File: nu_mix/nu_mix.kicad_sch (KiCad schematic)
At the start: 63 parts, among them J1 2X5, J2 I/O connector, J3 I/O connector, Q1 LBSS84LT1G, SW1 SW_DP3T, SW2 SW_DP3T, SW3 SW_DP3T, SW4 SW_DP3T, SW5 SW_DP3T, SW6 SW_DP3T, SW7 SW_DP3T, SW8 SW_DP3T, U1 OPA202IDBVR, U2 OPA2202IDGKR

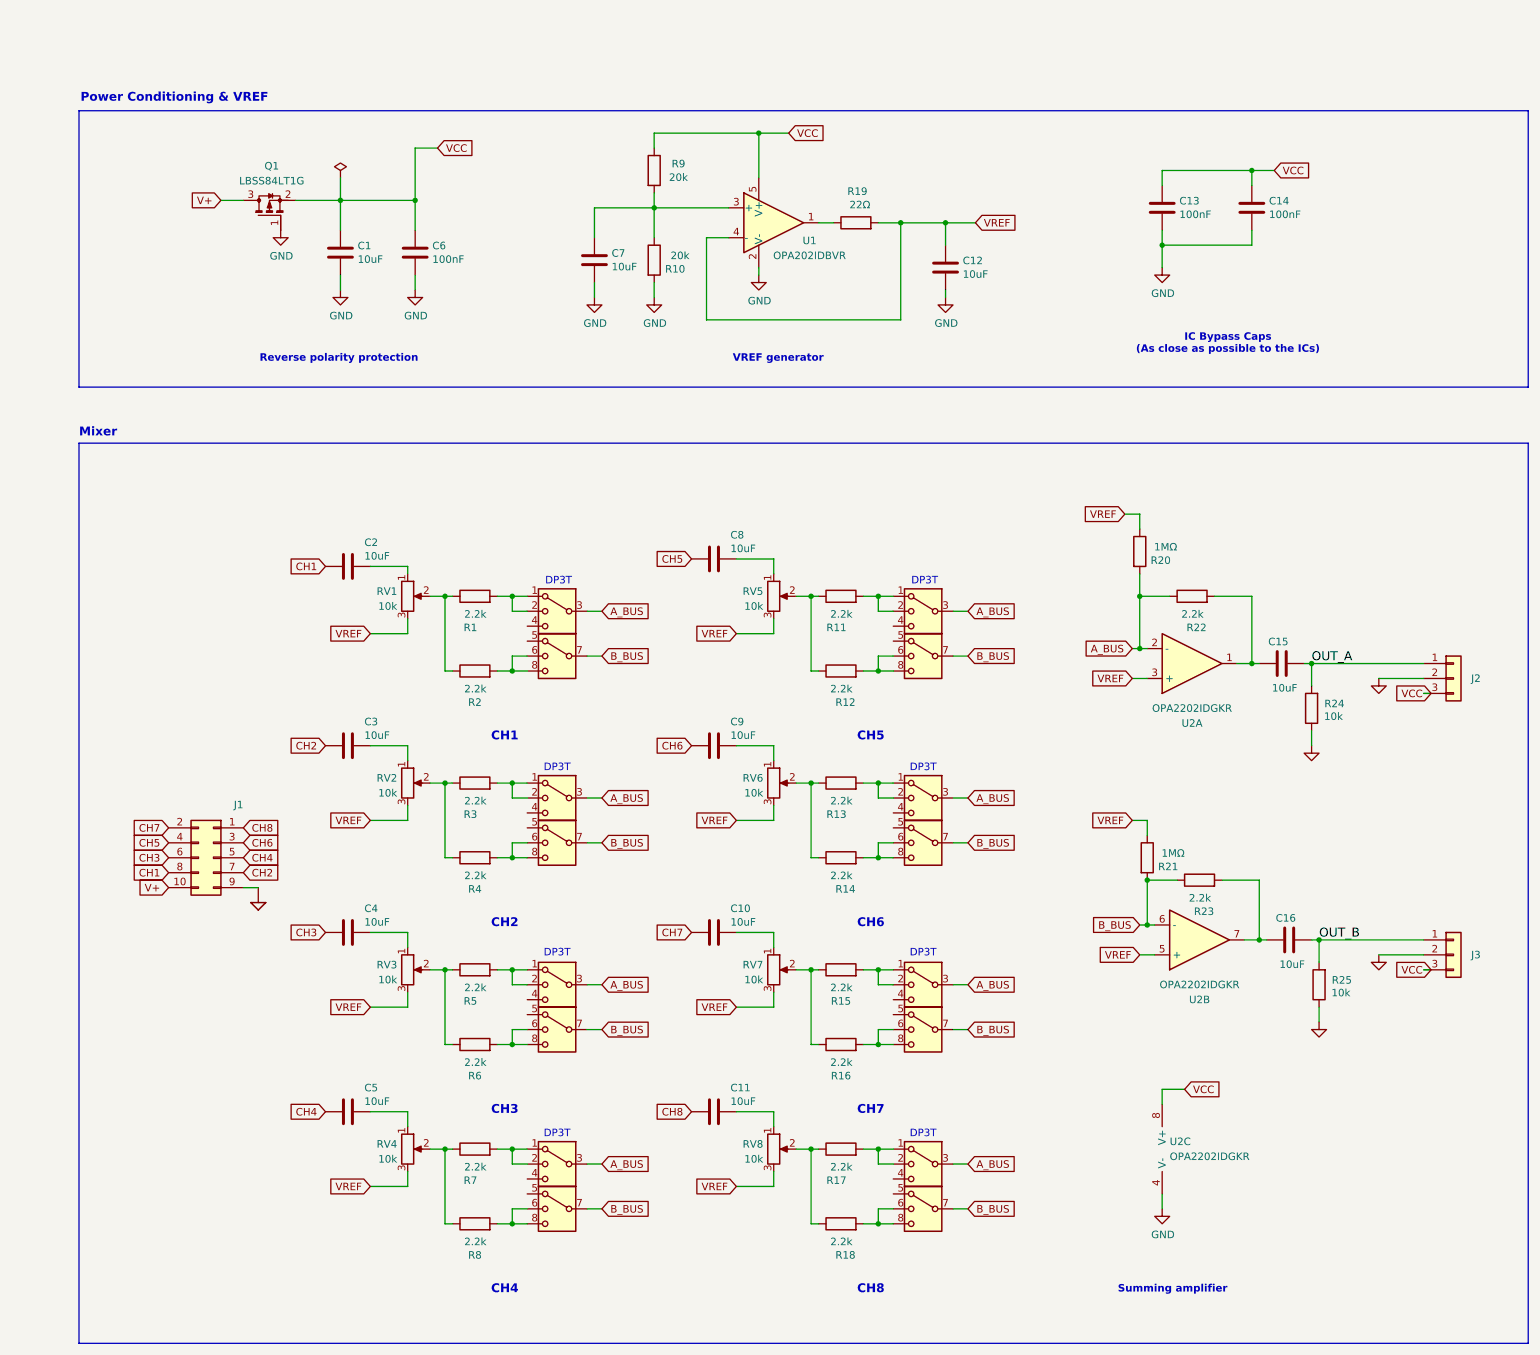
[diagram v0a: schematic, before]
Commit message: - Complete schematics - Start PCB layout - Switch to shorter 20mm sliders
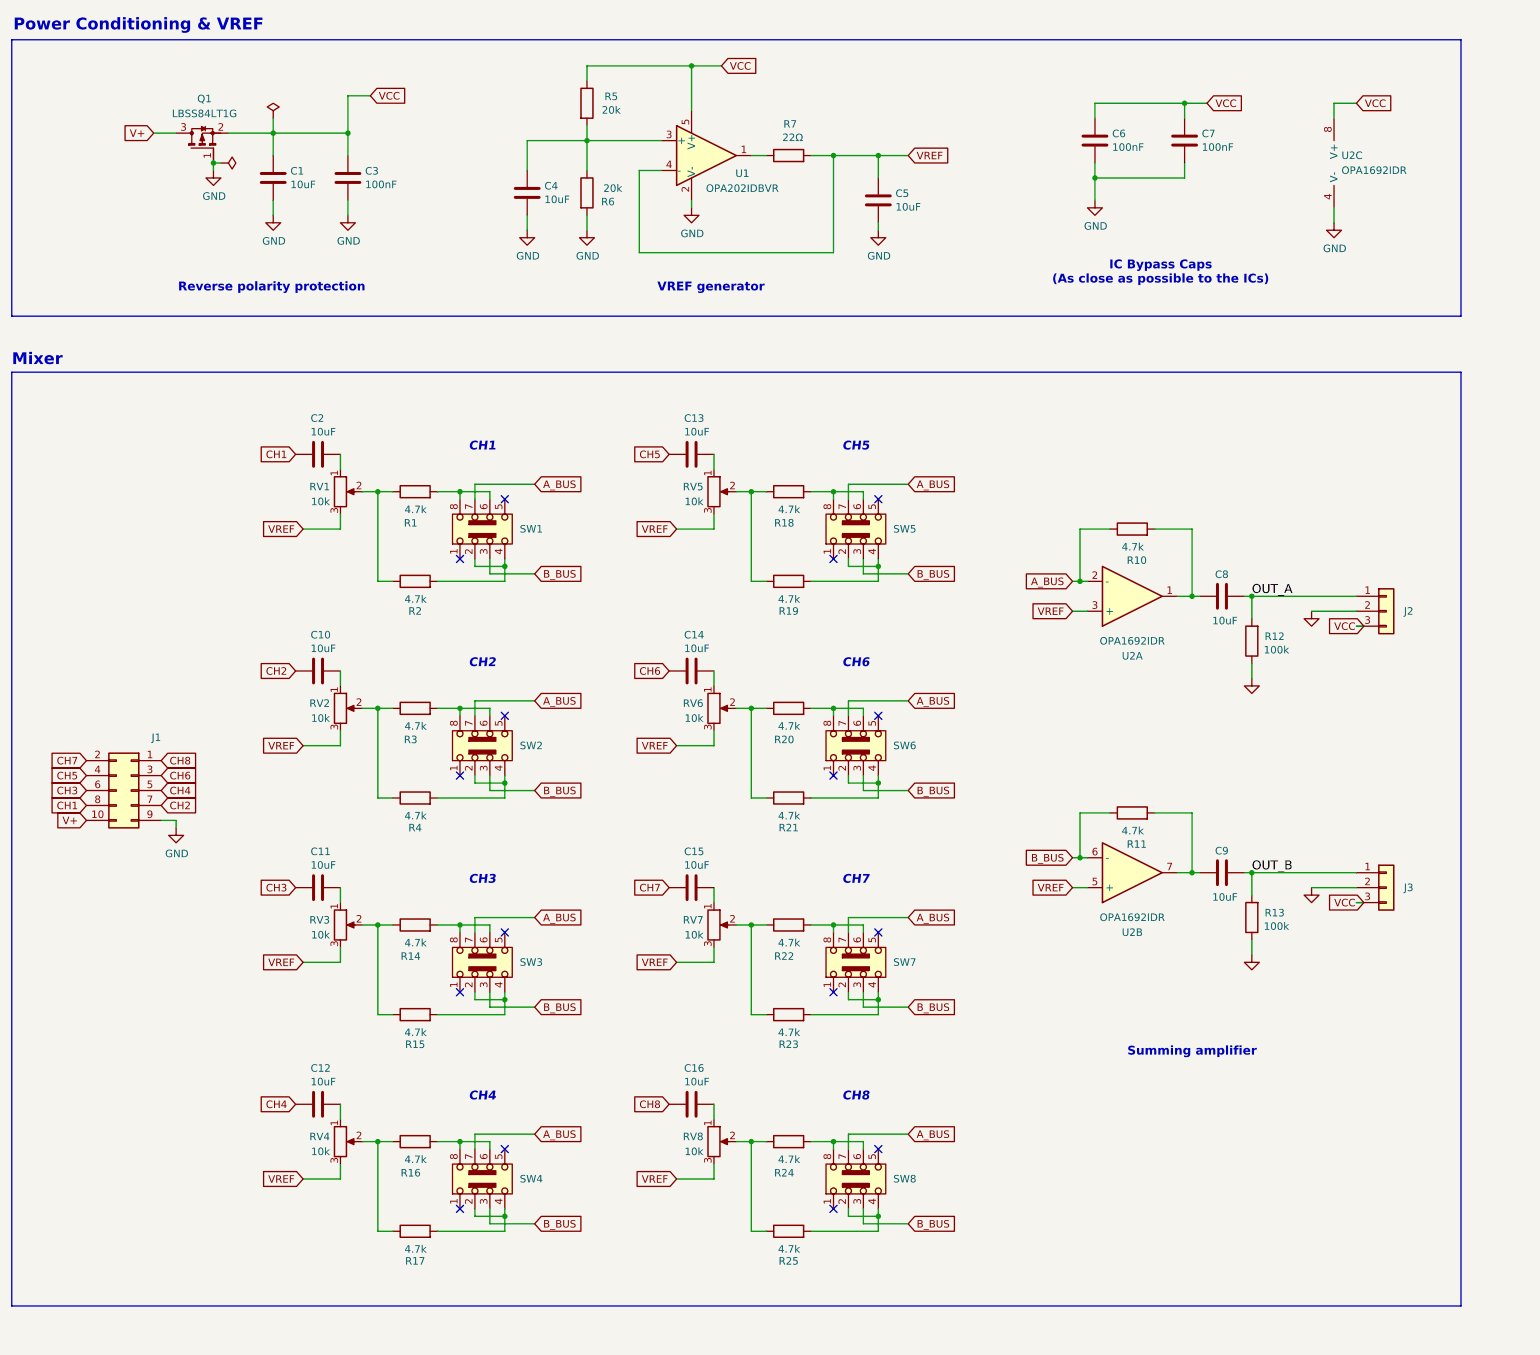
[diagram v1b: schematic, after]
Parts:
- removed C2, C3, C4, C5, C9: 10uF, Capacitor_SMD:C_0603_1608Metric, symbol Device:C
- removed R1, R13, R2, R5, R6, R7, R8: 2.2k, Resistor_SMD:R_0402_1005Metric, symbol Device:R
- removed RV1: 10k, cycfi_library:Alps_RS301111A01G, symbol Device:R_Potentiometer
- removed SW1, SW2, SW3, SW4, SW5, SW6, SW7, SW8: SW_DP3T, symbol Switch:SW_DP3T
- added C12, C13, C14, C15, C16: 10uF, Capacitor_SMD:C_0603_1608Metric, symbol Device:C
- added R19, R22, R23, R24, R25: 4.7k, Resistor_SMD:R_0402_1005Metric, symbol Device:R
- added RV5: 10k, cycfi_library:Alps_RS201111J011, symbol Device:R_Potentiometer
- added SW1, SW2, SW3, SW4, SW5, SW6, SW7, SW8: SW_Slide_DP3T, cycfi_library:K3-1400S-D1, symbol cycfi_library:SW_Slide_DP3T
- R1: renamed from R11; value 2.2k -> 4.7k; LCSC C25879 -> C25900
- R10: renamed from R22; value 2.2k -> 4.7k; LCSC C25879 -> C25900
- R11: renamed from R23; value 2.2k -> 4.7k; LCSC C25879 -> C25900
- R12: renamed from R24; value 10k -> 100k; LCSC C25744 -> C25741
- R13: renamed from R25; value 10k -> 100k; LCSC C25744 -> C25741
- R14, R15, R16, R17, R18, R3, R4: value 2.2k -> 4.7k; LCSC C25879 -> C25900
- R2: renamed from R12; value 2.2k -> 4.7k; LCSC C25879 -> C25900
- R20, R21: value 1MΩ -> 4.7k; LCSC C26083 -> C25900
- RV1: renamed from RV5; footprint cycfi_library:Alps_RS301111A01G -> cycfi_library:Alps_RS201111J011; LCSC (none) -> C255504
- RV2, RV3, RV4, RV6, RV7, RV8: footprint cycfi_library:Alps_RS301111A01G -> cycfi_library:Alps_RS201111J011; LCSC (none) -> C255504
- U1: LCSC (none) -> C1850244
- U2: value OPA2202IDGKR -> OPA1692IDR; footprint (none) -> Package_SO:SOIC-8_3.9x4.9mm_P1.27mm; LCSC (none) -> C2060550
- renumbered C8 to C2, C6 to C3, C7 to C4, C12 to C5, C13 to C6, C14 to C7, C15 to C8, C16 to C9, R9 to R5, R10 to R6, R19 to R7
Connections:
- net A_BUS: now also SW1.7 (C2), SW2.7 (C2), SW3.7 (C2), SW4.7 (C2), SW5.7 (C2), SW6.7 (C2), SW7.7 (C2), SW8.7 (C2); no longer R20.2
- net B_BUS: now also SW1.3 (C1`), SW2.3 (C1`), SW3.3 (C1`), SW4.3 (C1`), SW5.3 (C1`), SW6.3 (C1`), SW7.3 (C1`), SW8.3 (C1`); no longer R21.2
- net CH1: now also C2.1
- net CH2: now also C10.1
- net CH3: now also C11.1
- net CH4: now also C12.1
- net CH5: now also C13.1; no longer C2.1
- net CH6: now also C14.1
- net CH7: now also C15.1; no longer C10.1
- net CH8: now also C16.1; no longer C11.1
- net VREF: now also RV5.3; no longer R20.1, R21.1
- net at R3.2: now also SW2.6 (C2`), SW2.8 (A2)
- net at R16.2: now also SW4.6 (C2`), SW4.8 (A2)
- net at R4.2: now also SW2.2 (C1), SW2.4 (B1)
- net at RV4.2: now also R16.1, R17.1
- net at RV4.1: now also C12.2
- net at R17.2: now also SW4.2 (C1), SW4.4 (B1)
- net at R14.2: now also SW3.6 (C2`), SW3.8 (A2)
- net at R1.2: now also SW1.6 (C2`), SW1.8 (A2)
- net at C10.2: now also RV2.1; no longer RV7.1
- net at RV6.1: now also C14.2
- net at RV6.2: now also R20.1, R21.1; no longer R14.1
- net at RV8.1: now also C16.2; no longer C11.2
- net at R15.2: now also SW3.2 (C1), SW3.4 (B1)
- net at RV3.1: now also C11.2
- net at R18.2: now also SW5.6 (C2`), SW5.8 (A2)
- net at R2.2: now also SW1.2 (C1), SW1.4 (B1)
- net at RV3.2: now also R14.1, R15.1
- new net: R20.2, SW6.6 (C2`), SW6.8 (A2)
- new net: R23.2, SW7.2 (C1), SW7.4 (B1)
- new net: R22.2, SW7.6 (C2`), SW7.8 (A2)
- new net: R21.2, SW6.2 (C1), SW6.4 (B1)
- new net: R22.1, R23.1, RV7.2
- new net: C15.2, RV7.1
- new net: R18.1, R19.1, RV5.2
- new net: R19.2, SW5.2 (C1), SW5.4 (B1)
- new net: C13.2, RV5.1
- new net: R24.1, R25.1, RV8.2
- new net: R24.2, SW8.6 (C2`), SW8.8 (A2)
- new net: R25.2, SW8.2 (C1), SW8.4 (B1)
- no-connect marks 0 -> 16
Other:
- note removed: "DP3T"
- moved on the sheet: C1, C2, C3, C4, C5, C6, C7, C8, C9, J1, J2, J3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

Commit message: Full layout
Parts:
- J1: footprint Connector_PinHeader_2.00mm:PinHeader_2x05_P2.00mm_Vertical -> cycfi_library:pin_header_2x5p_2.54mm_smd_horizontal
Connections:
- net A_BUS: now also SW1.3 (C1`), SW2.3 (C1`), SW3.3 (C1`), SW4.3 (C1`), SW5.3 (C1`), SW6.3 (C1`), SW7.3 (C1`), SW8.3 (C1`); no longer SW1.7 (C2), SW2.7 (C2), SW3.7 (C2), SW4.7 (C2), SW5.7 (C2), SW6.7 (C2), SW7.7 (C2), SW8.7 (C2)
- net B_BUS: now also SW1.7 (C2), SW2.7 (C2), SW3.7 (C2), SW4.7 (C2), SW5.7 (C2), SW6.7 (C2), SW7.7 (C2), SW8.7 (C2); no longer SW1.3 (C1`), SW2.3 (C1`), SW3.3 (C1`), SW4.3 (C1`), SW5.3 (C1`), SW6.3 (C1`), SW7.3 (C1`), SW8.3 (C1`)
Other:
- moved on the sheet: R1, R14, R15, R16, R17, R18, R19, R2, R20, R21, R22, R23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

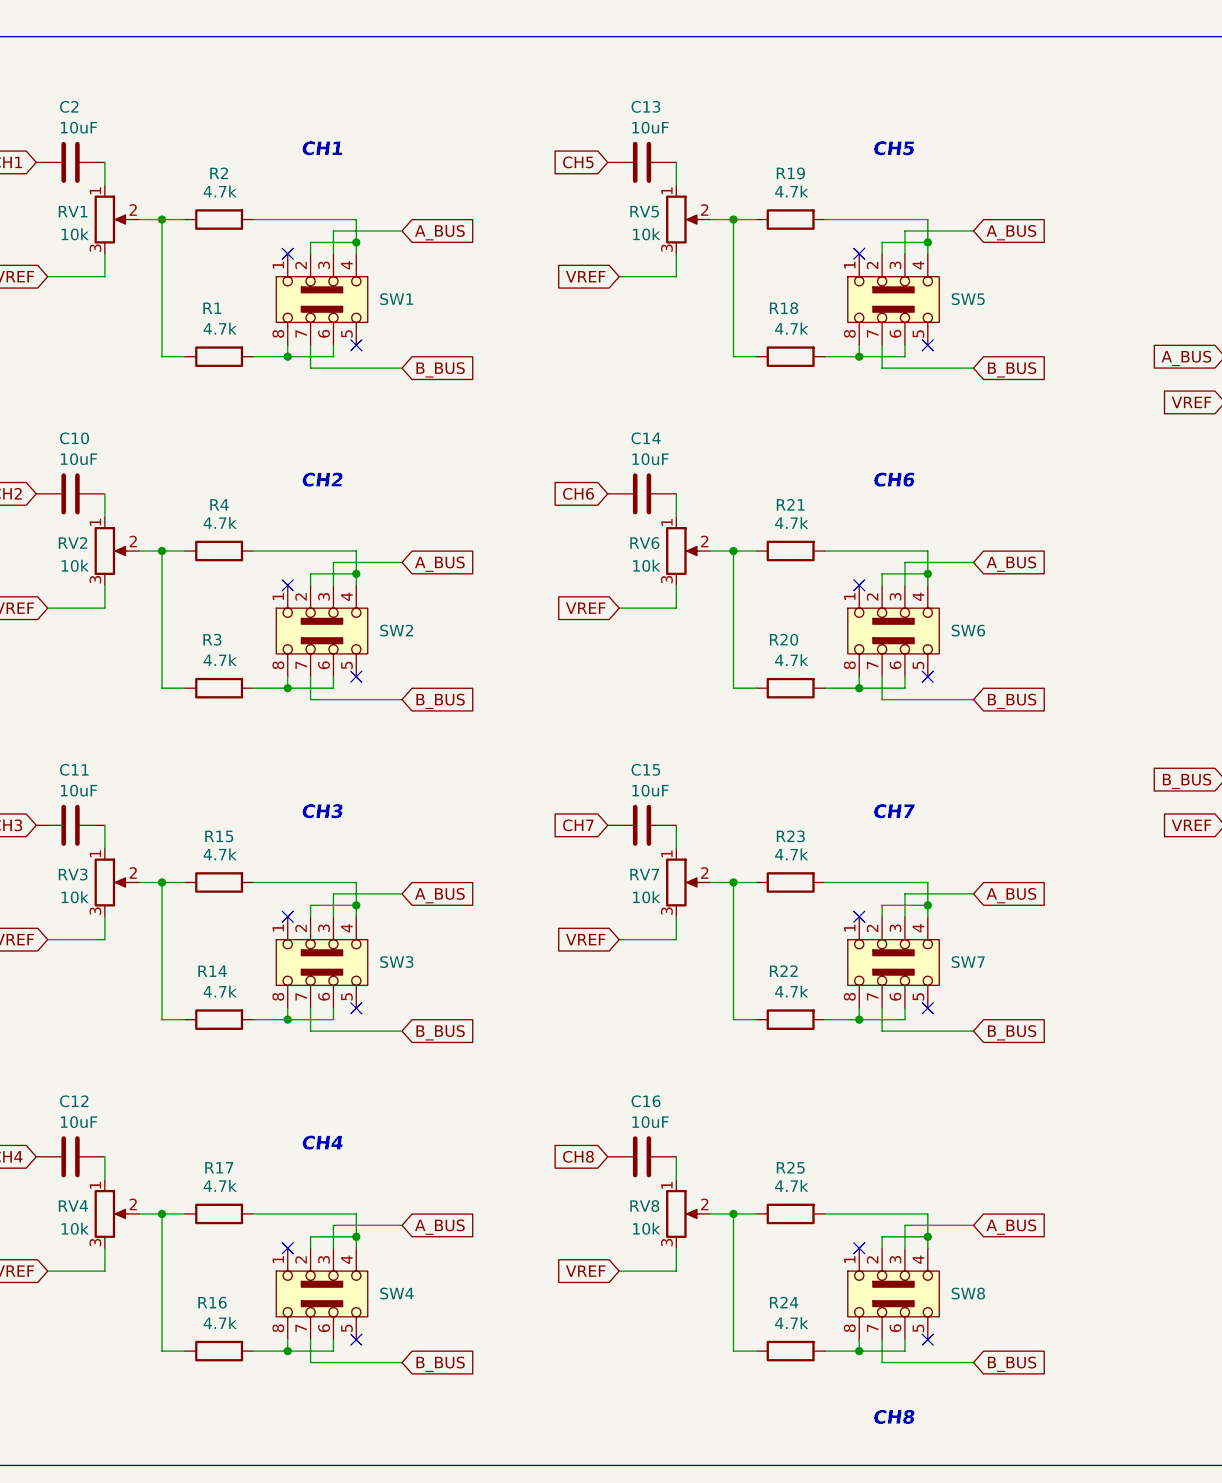
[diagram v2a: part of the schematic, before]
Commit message: Fix orientation of the slide switches so A is at the left and B is at the right in both the schematic diagram and the PCB
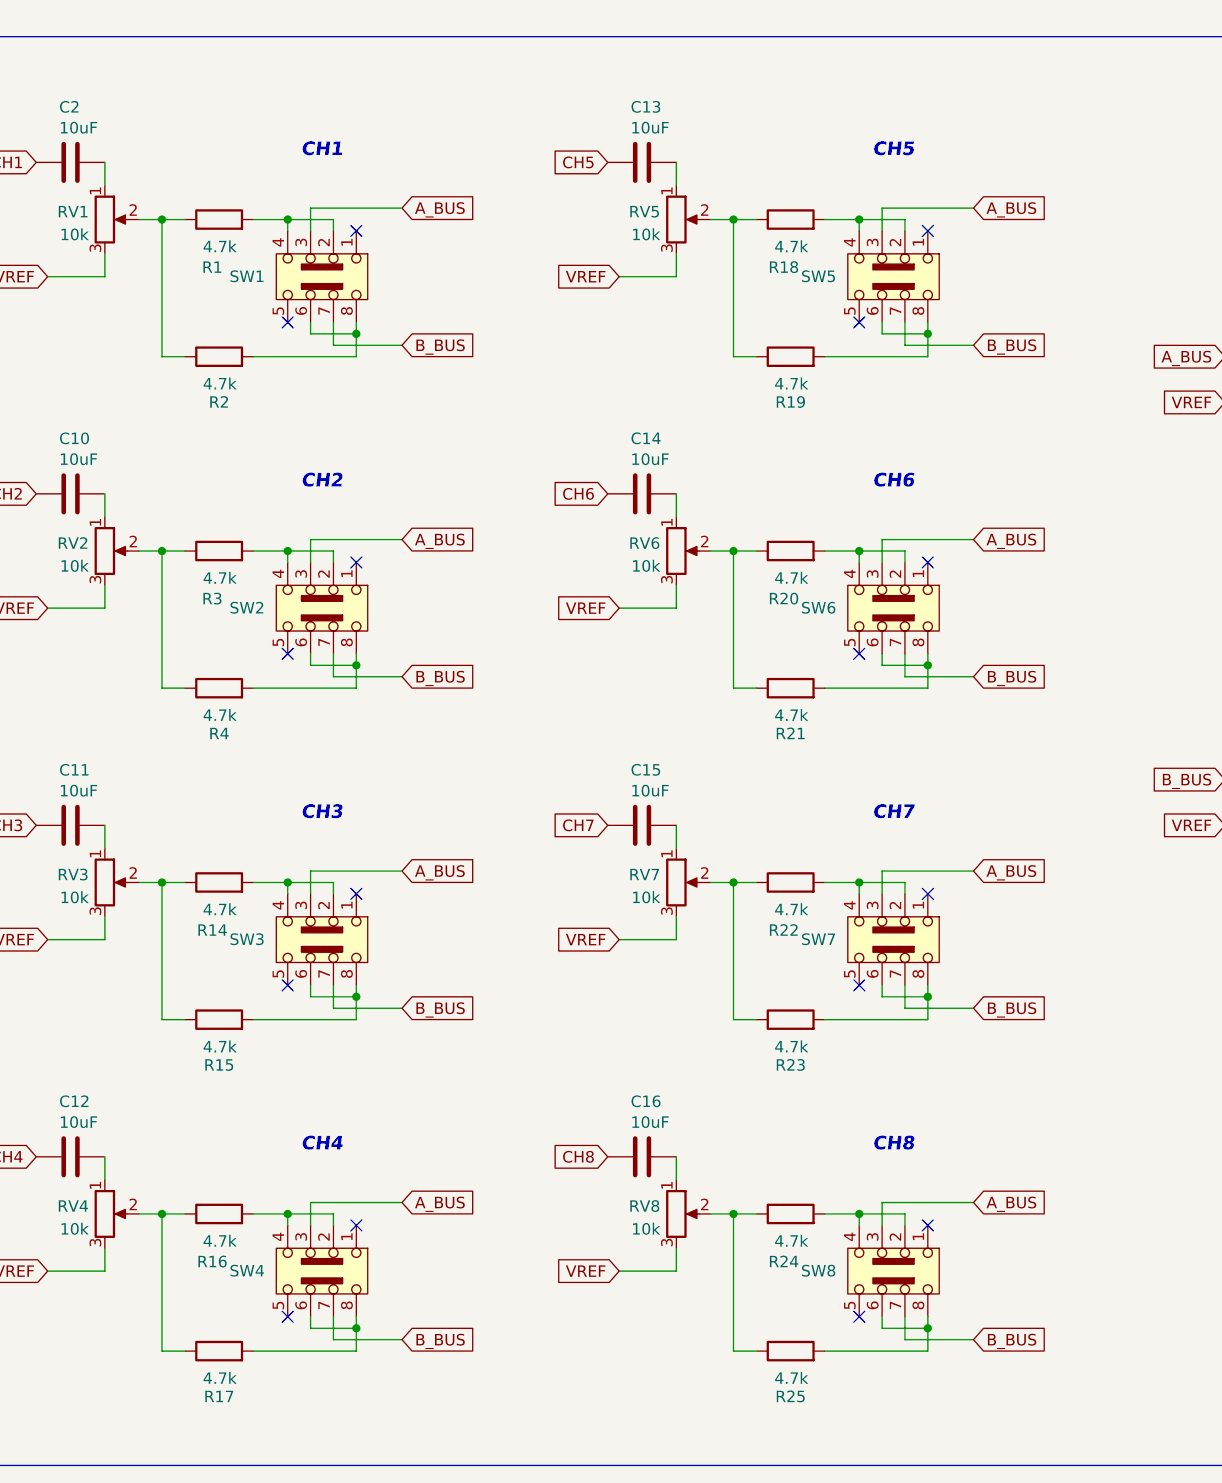
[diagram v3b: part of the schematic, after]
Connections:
- net at SW6.6 (C2`), SW6.8 (A2): now also R21.2; no longer R20.2
- net at SW7.2 (C1), SW7.4 (B1): now also R22.2; no longer R23.2
- net at SW7.6 (C2`), SW7.8 (A2): now also R23.2; no longer R22.2
- net at SW6.2 (C1), SW6.4 (B1): now also R20.2; no longer R21.2
- net at SW5.2 (C1), SW5.4 (B1): now also R18.2; no longer R19.2
- net at SW1.6 (C2`), SW1.8 (A2): now also R2.2; no longer R1.2
- net at SW2.2 (C1), SW2.4 (B1): now also R3.2; no longer R4.2
- net at SW2.6 (C2`), SW2.8 (A2): now also R4.2; no longer R3.2
- net at SW4.2 (C1), SW4.4 (B1): now also R16.2; no longer R17.2
- net at SW4.6 (C2`), SW4.8 (A2): now also R17.2; no longer R16.2
- net at SW3.2 (C1), SW3.4 (B1): now also R14.2; no longer R15.2
- net at SW3.6 (C2`), SW3.8 (A2): now also R15.2; no longer R14.2
- net at SW8.6 (C2`), SW8.8 (A2): now also R25.2; no longer R24.2
- net at SW5.6 (C2`), SW5.8 (A2): now also R19.2; no longer R18.2
- net at SW8.2 (C1), SW8.4 (B1): now also R24.2; no longer R25.2
- net at SW1.2 (C1), SW1.4 (B1): now also R1.2; no longer R2.2
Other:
- moved on the sheet: R1, R14, R15, R16, R17, R18, R19, R2, R20, R21, R22, R23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
